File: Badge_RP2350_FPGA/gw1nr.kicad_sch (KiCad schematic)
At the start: 23 parts, among them U2 GW1N-LV9QN88C6_I5_, U4 W25Q128JVS

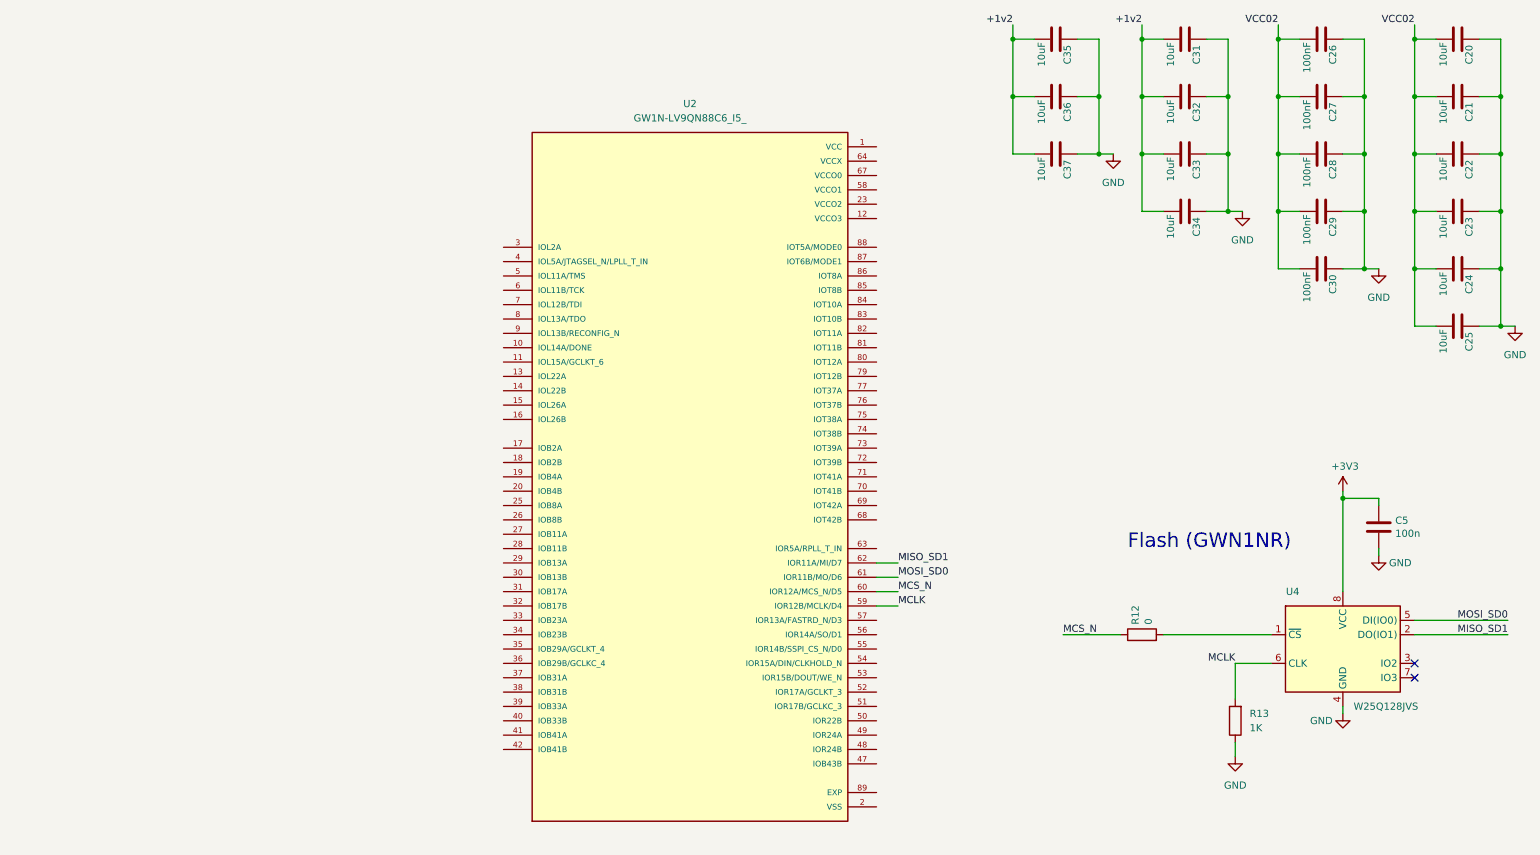
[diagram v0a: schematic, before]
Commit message: add jtag connection
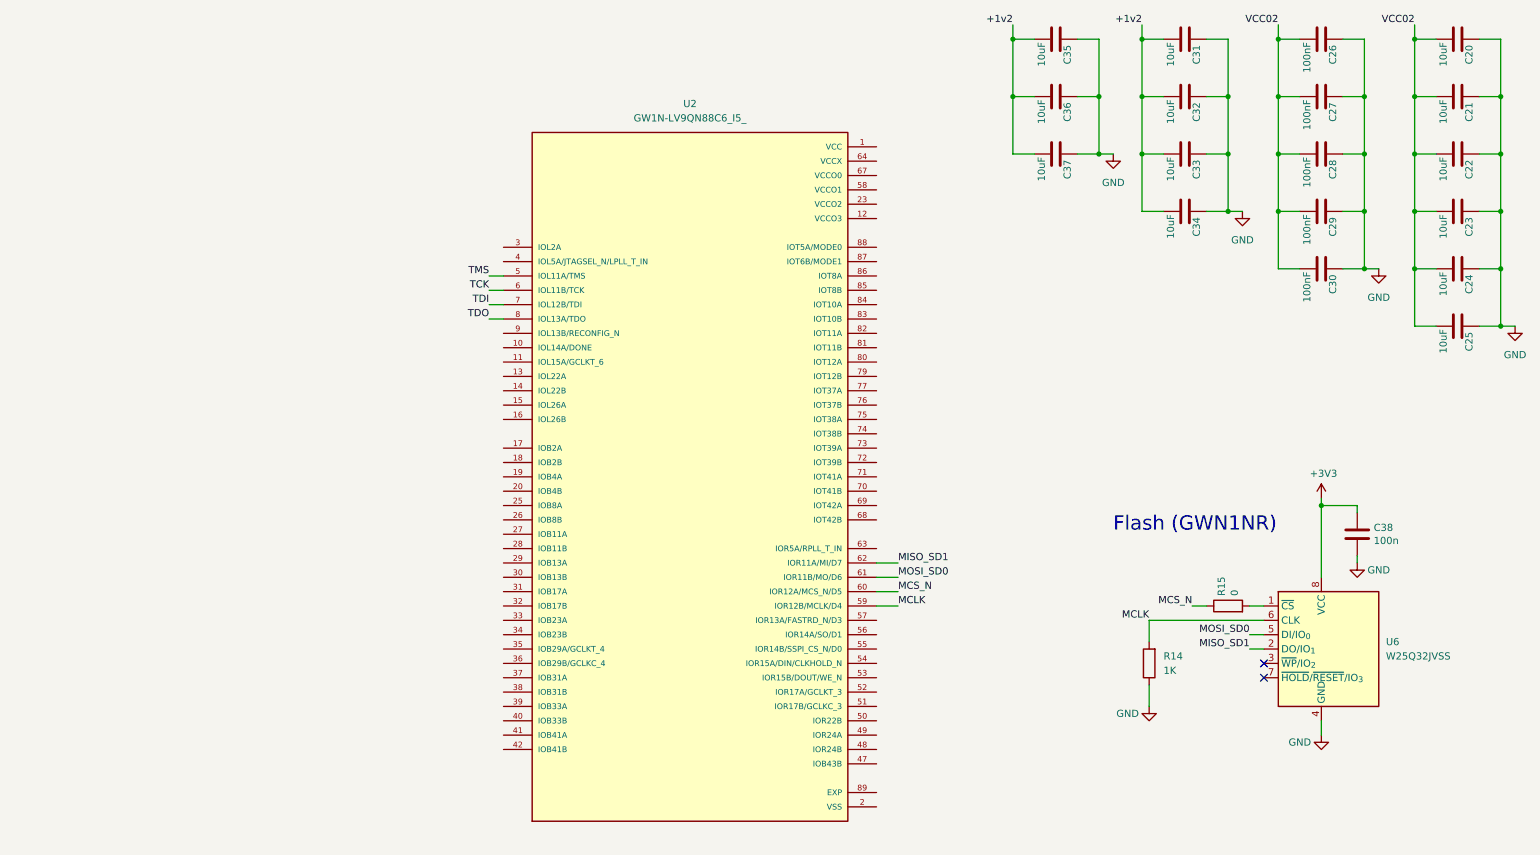
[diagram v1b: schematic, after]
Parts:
- removed C5: 100n, Capacitor_SMD:C_0402_1005Metric, symbol Device:C
- removed R12: 0, Resistor_SMD:R_0402_1005Metric, symbol Device:R
- removed R13: 1K, symbol Device:R
- removed U4: W25Q128JVS, Package_SO:SOIC-8_5.23x5.23mm_P1.27mm, symbol Memory_Flash:W25Q128JVS
- added C38: 100n, Capacitor_SMD:C_0402_1005Metric, symbol Device:C
- added R14: 1K, symbol Device:R
- added R15: 0, Resistor_SMD:R_0402_1005Metric, symbol Device:R
- added U6: W25Q32JVSS, Package_SO:SOIC-8_5.3x5.3mm_P1.27mm, symbol Memory_Flash:W25Q32JVSS
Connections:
- net +3V3: now also C38.1, U6.8 (VCC)
- net GND: now also C38.2, R14.1, U6.4 (GND)
- net MCLK: now also R14.2, U6.6 (CLK)
- net MCS_N: now also R15.1
- net MISO_SD1: now also U6.2 (DO/IO_{1})
- net MOSI_SD0: now also U6.5 (DI/IO_{0})
- net TMS: now reaches U2.5 (IOL11A/TMS)
- net TCK: now reaches U2.6 (IOL11B/TCK)
- net TDI: now reaches U2.7 (IOL12B/TDI)
- net TDO: now reaches U2.8 (IOL13A/TDO)
- new net: R15.2, U6.1 (~{CS})

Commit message: add buttons by Arianna and make Flash 2 shared between 2 chips
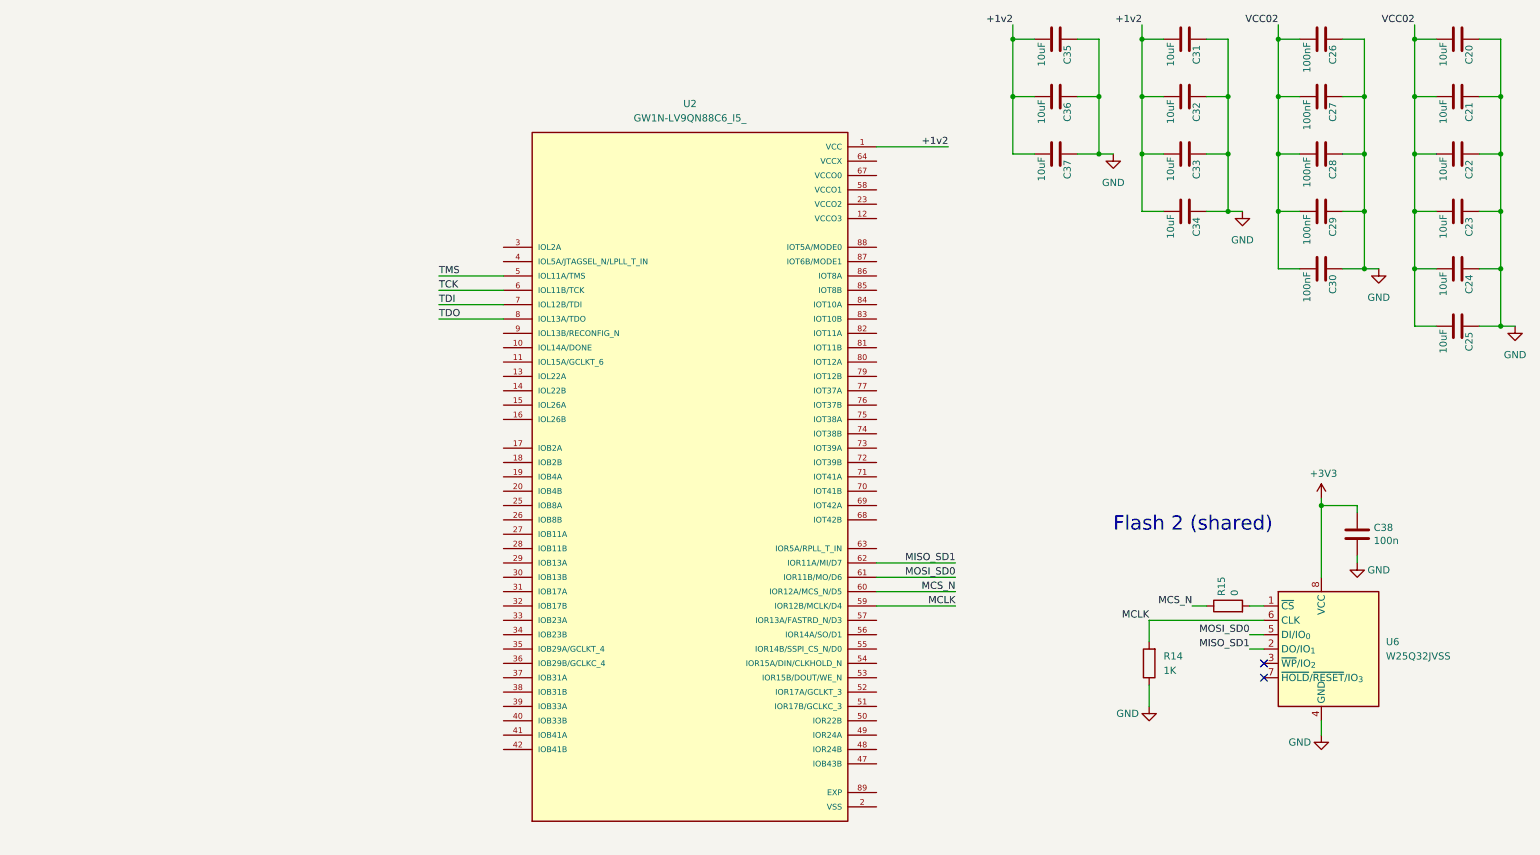
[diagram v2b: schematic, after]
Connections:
- net +1v2 is gone; now on net VCC: C31.2, C32.2, C33.2, C34.2, C35.2, C36.2, C37.2
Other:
- note added: "Flash 2 (shared)"
- note removed: "Flash (GWN1NR)"
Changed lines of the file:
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@@
 	(generator_version "10.0")
 	(paper "A4")
-	(text "Flash (GWN1NR)"
+	(text "Flash 2 (shared)"
 		(exclude_from_sim no)
 		(at 208.28 111.506 0)
@@
 	(wire
 		(pts
+			(xy 166.37 43.18) (xy 179.07 43.18)
+		)
+		(stroke
+			(width 0)
+			(type default)
+		)
+	)
+	(wire
+		(pts
 			(xy 245.11 106.68) (xy 245.11 119.38)
 		)
@@
 	(wire
 		(pts
-			(xy 166.37 124.46) (xy 170.18 124.46)
-		)
-		(stroke
-			(width 0)
-			(type default)
-		)
-	)
-	(wire
-		(pts
 			(xy 261.62 34.29) (xy 261.62 44.45)
 		)
@@
 	(wire
 		(pts
+			(xy 166.37 116.84) (xy 180.34 116.84)
+		)
+		(stroke
+			(width 0)
+			(type default)
+		)
+	)
+	(wire
+		(pts
 			(xy 237.49 54.61) (xy 237.49 64.77)
 		)
@@
 	(wire
 		(pts
-			(xy 97.79 68.58) (xy 100.33 68.58)
+			(xy 88.9 68.58) (xy 100.33 68.58)
 		)
 		(stroke
@@
 	(wire
 		(pts
-			(xy 166.37 119.38) (xy 170.18 119.38)
-		)
-		(stroke
-			(width 0)
-			(type default)
-		)
-	)
-	(wire
-		(pts
 			(xy 265.43 34.29) (xy 261.62 34.29)
 		)
@@
 	(wire
 		(pts
+			(xy 166.37 124.46) (xy 180.34 124.46)
+		)
+		(stroke
+			(width 0)
+			(type default)
+		)
+	)
+	(wire
+		(pts
 			(xy 252.73 34.29) (xy 252.73 44.45)
 		)
@@
 	(wire
 		(pts
+			(xy 166.37 121.92) (xy 180.34 121.92)
+		)
+		(stroke
+			(width 0)
+			(type default)
+		)
+	)
+	(wire
+		(pts
 			(xy 217.17 44.45) (xy 213.36 44.45)
 		)
@@
 	(wire
 		(pts
-			(xy 166.37 121.92) (xy 170.18 121.92)
-		)
-		(stroke
-			(width 0)
-			(type default)
-		)
-	)
-	(wire
-		(pts
 			(xy 237.49 21.59) (xy 237.49 24.13)
 		)
@@
 	(wire
 		(pts
+			(xy 166.37 119.38) (xy 180.34 119.38)
+		)
+		(stroke
+			(width 0)
+			(type default)
+		)
+	)
+	(wire
+		(pts
 			(xy 205.74 34.29) (xy 201.93 34.29)
 		)
@@
 	(wire
 		(pts
-			(xy 97.79 66.04) (xy 100.33 66.04)
+			(xy 88.9 66.04) (xy 100.33 66.04)
 		)
 		(stroke
@@
 	(wire
 		(pts
-			(xy 97.79 73.66) (xy 100.33 73.66)
+			(xy 88.9 73.66) (xy 100.33 73.66)
 		)
 		(stroke
@@
 	(wire
 		(pts
-			(xy 97.79 71.12) (xy 100.33 71.12)
-		)
-		(stroke
-			(width 0)
-			(type default)
-		)
-	)
-	(wire
-		(pts
-			(xy 166.37 116.84) (xy 170.18 116.84)
+			(xy 88.9 71.12) (xy 100.33 71.12)
 		)
 		(stroke
@@
 	)
 	(label "MISO_SD1"
-		(at 170.18 116.84 0)
-		(effects
-			(font
-				(size 1.27 1.27)
-			)
-			(justify left bottom)
+		(at 180.34 116.84 180)
+		(effects
+			(font
+				(size 1.27 1.27)
+			)
+			(justify right bottom)
 		)
 	)
 	(label "MCS_N"
-		(at 170.18 121.92 0)
-		(effects
-			(font
-				(size 1.27 1.27)
-			)
-			(justify left bottom)
+		(at 180.34 121.92 180)
+		(effects
+			(font
+				(size 1.27 1.27)
+			)
+			(justify right bottom)
 		)
 	)
 	(label "MCLK"
-		(at 170.18 124.46 0)
-		(effects
-			(font
-				(size 1.27 1.27)
-			)
-			(justify left bottom)
+		(at 180.34 124.46 180)
+		(effects
+			(font
+				(size 1.27 1.27)
+			)
+			(justify right bottom)
 		)
 	)
@@
 	)
 	(label "MOSI_SD0"
-		(at 170.18 119.38 0)
+		(at 180.34 119.38 180)
+		(effects
+			(font
+				(size 1.27 1.27)
+			)
+			(justify right bottom)
+		)
+	)
+	(label "TMS"
+		(at 88.9 66.04 0)
 		(effects
 			(font
@@
 		)
 	)
-	(label "TMS"
-		(at 97.79 66.04 180)
-		(effects
-			(font
-				(size 1.27 1.27)
-			)
-			(justify right bottom)
-		)
-	)
 	(label "TDI"
-		(at 97.79 71.12 180)
-		(effects
-			(font
-				(size 1.27 1.27)
-			)
-			(justify right bottom)
+		(at 88.9 71.12 0)
+		(effects
+			(font
+				(size 1.27 1.27)
+			)
+			(justify left bottom)
 		)
 	)
@@
 	)
 	(label "TDO"
-		(at 97.79 73.66 180)
-		(effects
-			(font
-				(size 1.27 1.27)
-			)
-			(justify right bottom)
+		(at 88.9 73.66 0)
+		(effects
+			(font
+				(size 1.27 1.27)
+			)
+			(justify left bottom)
 		)
 	)
@@
 		)
 	)
+	(label "+1v2"
+		(at 179.07 43.18 180)
+		(effects
+			(font
+				(size 1.27 1.27)
+			)
+			(justify right bottom)
+		)
+	)
 	(label "TCK"
-		(at 97.79 68.58 180)
-		(effects
-			(font
-				(size 1.27 1.27)
-			)
-			(justify right bottom)
-		)
-	)
+		(at 88.9 68.58 0)
+		(effects
+			(font
+				(size 1.27 1.27)
+			)
+			(justify left bottom)
+		)
+	)

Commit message: delete Core directory - not the right repository
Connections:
- net GPIO1: now reaches U2.87 (IOT6B/MODE1)
- net GPIO0: now reaches U2.88 (IOT5A/MODE0)
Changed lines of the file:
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@@
+	(wire
+		(pts
+			(xy 166.37 60.96) (xy 179.07 60.96)
+		)
+		(stroke
+			(width 0)
+			(type default)
+		)
+	)
 	(wire
 		(pts
@@
 		(pts
 			(xy 276.86 64.77) (xy 276.86 74.93)
+		)
+		(stroke
+			(width 0)
+			(type default)
+		)
+	)
+	(wire
+		(pts
+			(xy 166.37 63.5) (xy 179.07 63.5)
 		)
 		(stroke
@@
 		)
 	)
+	(label "GPIO1"
+		(at 179.07 63.5 180)
+		(effects
+			(font
+				(size 1.27 1.27)
+			)
+			(justify right bottom)
+		)
+	)
 	(label "TDI"
 		(at 88.9 71.12 0)
@@
 		(effects
 			(font
+				(size 1.27 1.27)
+			)
+			(justify right bottom)
+		)
+	)
+	(label "GPIO0"
+		(at 179.07 60.96 180)
+		(effects
+			(font

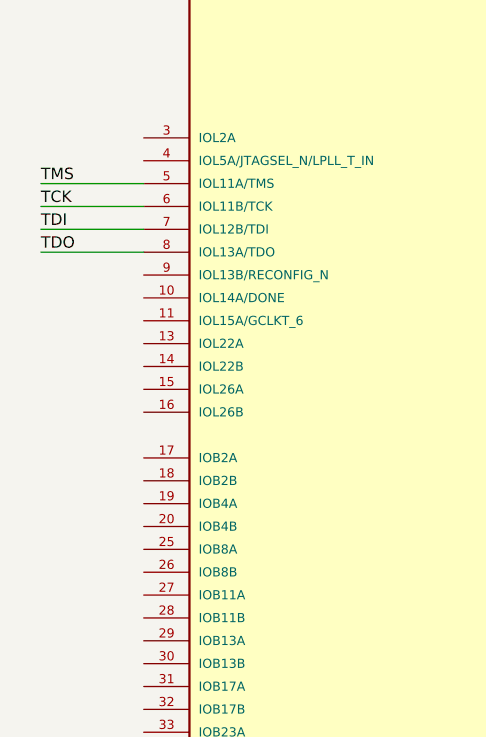
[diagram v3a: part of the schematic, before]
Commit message: add type c port and uart connections
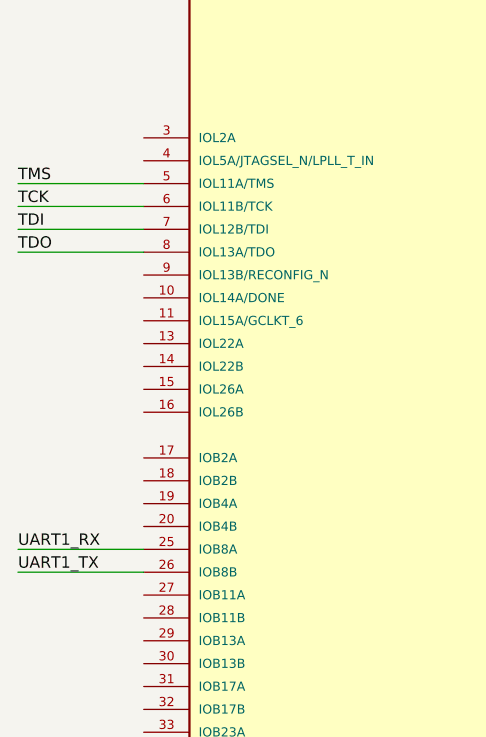
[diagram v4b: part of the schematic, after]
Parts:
- C20, C21, C22, C23, C24, C25, C26, C27, C28, C29, C30, C31, C32, C33, C34, C35, C36, C37: footprint (none) -> Capacitor_SMD:C_0402_1005Metric
- R14: footprint (none) -> Resistor_THT:R_Axial_DIN0204_L3.6mm_D1.6mm_P1.90mm_Vertical
- U2: footprint GW1N-LV9QN88C6_I5_:QFN40P1000X1000X95-89N -> semitovpartslibrary:QFN40P1000X1000X95-89N
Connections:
- net UART1_RX: now reaches U2.25 (IOB8A)
- net UART1_TX: now reaches U2.26 (IOB8B)
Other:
- company: (none) -> SemiTO-V, RISC-V Student Team
- title: (none) -> RISC-V Summit Europe Badge
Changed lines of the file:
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@@
 	(generator_version "10.0")
 	(paper "A4")
+	(title_block
+		(title "RISC-V Summit Europe Badge")
+		(date "2026-03-29")
+		(rev "v1.0")
+		(company "SemiTO-V, RISC-V Student Team")
+		(comment 3 "License: CERN-OHL-W")
+		(comment 4 "Authors: Tan Siret Akıncı, Alessandro Bochino, Carlo Bendelli, Arianna Bruno")
+	)
 	(text "Flash 2 (shared)"
 		(exclude_from_sim no)
@@
 	(wire
 		(pts
-			(xy 88.9 68.58) (xy 100.33 68.58)
+			(xy 86.36 68.58) (xy 100.33 68.58)
 		)
 		(stroke
@@
 	(wire
 		(pts
+			(xy 86.36 109.22) (xy 100.33 109.22)
+		)
+		(stroke
+			(width 0)
+			(type default)
+		)
+	)
+	(wire
+		(pts
 			(xy 252.73 54.61) (xy 248.92 54.61)
 		)
@@
 	(wire
 		(pts
-			(xy 88.9 66.04) (xy 100.33 66.04)
+			(xy 86.36 66.04) (xy 100.33 66.04)
 		)
 		(stroke
@@
 	(wire
 		(pts
-			(xy 88.9 73.66) (xy 100.33 73.66)
+			(xy 86.36 73.66) (xy 100.33 73.66)
 		)
 		(stroke
@@
 	(wire
 		(pts
+			(xy 86.36 106.68) (xy 100.33 106.68)
+		)
+		(stroke
+			(width 0)
+			(type default)
+		)
+	)
+	(wire
+		(pts
 			(xy 205.74 24.13) (xy 205.74 34.29)
 		)
@@
 	(wire
 		(pts
-			(xy 88.9 71.12) (xy 100.33 71.12)
+			(xy 86.36 71.12) (xy 100.33 71.12)
 		)
 		(stroke
@@
 		)
 	)
+	(label "UART1_TX"
+		(at 86.36 109.22 0)
+		(effects
+			(font
+				(size 1.27 1.27)
+			)
+			(justify left bottom)
+		)
+	)
+	(label "UART1_RX"
+		(at 86.36 106.68 0)
+		(effects
+			(font
+				(size 1.27 1.27)
+			)
+			(justify left bottom)
+		)
+	)
 	(label "TMS"
-		(at 88.9 66.04 0)
+		(at 86.36 66.04 0)
 		(effects
 			(font
@@
 	)
 	(label "TDI"
-		(at 88.9 71.12 0)
+		(at 86.36 71.12 0)
 		(effects
 			(font
@@
 	)
 	(label "TDO"
-		(at 88.9 73.66 0)
+		(at 86.36 73.66 0)
 		(effects
 			(font
@@
 	)
 	(label "TCK"
-		(at 88.9 68.58 0)
+		(at 86.36 68.58 0)
 		(effects
 			(font
@@
 			)
 		)
-		(property "Footprint" ""
+		(property "Footprint" "Capacitor_SMD:C_0402_1005Metric"
 			(at 241.3 55.5752 0)
 			(hide yes)
@@
 			)
 		)
-		(property "Footprint" ""
+		(property "Footprint" "Capacitor_SMD:C_0402_1005Metric"
 			(at 194.31 45.4152 0)
 			(hide yes)
@@
 			)
 		)
-		(property "Footprint" ""
+		(property "Footprint" "Capacitor_SMD:C_0402_1005Metric"
 			(at 194.31 25.0952 0)
 			(hide yes)
@@
 			)
 		)
-		(property "Footprint" ""
+		(property "Footprint" "Capacitor_SMD:C_0402_1005Metric"
 			(at 265.43 25.0952 0)
 			(hide yes)
@@
 			)
 		)
-		(property "Footprint" ""
+		(property "Footprint" "Capacitor_SMD:C_0402_1005Metric"
 			(at 241.3 25.0952 0)
 			(hide yes)
@@
 			)
 		)
-		(property "Footprint" ""
+		(property "Footprint" "Capacitor_SMD:C_0402_1005Metric"
 			(at 241.3 45.4152 0)
 			(hide yes)
@@
 			)
 		)
-		(property "Footprint" ""
+		(property "Footprint" "Capacitor_SMD:C_0402_1005Metric"
 			(at 265.43 45.4152 0)
 			(hide yes)
@@
 			)
 		)
-		(property "Footprint" ""
+		(property "Footprint" "Capacitor_SMD:C_0402_1005Metric"
 			(at 265.43 55.5752 0)
 			(hide yes)
@@
 			)
 		)
-		(property "Footprint" ""
+		(property "Footprint" "Capacitor_SMD:C_0402_1005Metric"
 			(at 194.31 35.2552 0)
 			(hide yes)
@@
 			)
 		)
-		(property "Footprint" ""
+		(property "Footprint" "Capacitor_SMD:C_0402_1005Metric"
 			(at 241.3 35.2552 0)
 			(hide yes)
@@
 			)
 		)
-		(property "Footprint" ""
+		(property "Footprint" "Capacitor_SMD:C_0402_1005Metric"
 			(at 217.17 55.5752 0)
 			(hide yes)
@@
 			)
 		)
-		(property "Footprint" ""
+		(property "Footprint" "Capacitor_SMD:C_0402_1005Metric"
 			(at 217.17 25.0952 0)
 			(hide yes)
@@
 			)
 		)
-		(property "Footprint" ""
+		(property "Footprint" "Capacitor_SMD:C_0402_1005Metric"
 			(at 217.17 35.2552 0)
 			(hide yes)
@@
 			)
 		)
-		(property "Footprint" ""
+		(property "Footprint" "Resistor_THT:R_Axial_DIN0204_L3.6mm_D1.6mm_P1.90mm_Vertical"
 			(at 216.408 134.62 90)
 			(hide yes)
@@
 			)
 		)
-		(property "Footprint" ""
+		(property "Footprint" "Capacitor_SMD:C_0402_1005Metric"
 			(at 241.3 65.7352 0)
 			(hide yes)
@@
 			)
 		)
-		(property "Footprint" ""
+		(property "Footprint" "Capacitor_SMD:C_0402_1005Metric"
 			(at 217.17 45.4152 0)
 			(hide yes)
@@
 			)
 		)
-		(property "Footprint" ""
+		(property "Footprint" "Capacitor_SMD:C_0402_1005Metric"
 			(at 265.43 75.8952 0)
 			(hide yes)
@@
 			)
 		)
-		(property "Footprint" "GW1N-LV9QN88C6_I5_:QFN40P1000X1000X95-89N"
+		(property "Footprint" "semitovpartslibrary:QFN40P1000X1000X95-89N"
 			(at 133.35 101.6 0)
 			(hide yes)
@@
 			)
 		)
-		(property "Footprint" ""
+		(property "Footprint" "Capacitor_SMD:C_0402_1005Metric"
 			(at 265.43 35.2552 0)
 			(hide yes)
@@
 			)
 		)
-		(property "Footprint" ""
+		(property "Footprint" "Capacitor_SMD:C_0402_1005Metric"
 			(at 265.43 65.7352 0)
 			(hide yes)
